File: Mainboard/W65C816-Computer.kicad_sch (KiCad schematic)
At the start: 103 parts, among them J1 ADDR_DATA_DBG, J2 CTRL_BANK_DBG, J3 CPU_MISC_DBG, J4 PJ-102A, J5 DAUGHTER_PWR_AUX, J6 ISA16_DAUGHTER_BUS, Q1 P-MOSFET_REV_PROT_TO220, SW1 RESET, SW2 NMI, SW3 MAIN_PWR_SW_EXT, U1 W65C816S6PG-14, U10 SN74HC04N, U11 SN74HC08N, U12 SN74HC139N, U2 SN74HC573N, U20 AS6C1008-55PCN, U21 AS6C1008-55PCN, U22 AS6C1008-55PCN, U23 AS6C1008-55PCN, U24 AS6C4008-55PCN, U25 AS6C4008-55PCN, U26 AS6C4008-55PCN, U27 AS6C4008-55PCN, U3 SN74HC245N, U30 SST39VF040-70-4I-NHE, U4 MCP130-315D, U5 SN74HC14N, U6 SN74HC138N, U7 SN74HC138N, U8 SN74HC138N, U9 SN74HC00N, X1 ECS-P143X-8.000-BN

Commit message: Added 4MiB memory back
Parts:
- U20, U21, U22, U23: value AS6C1008-55PCN -> AS6C4008-55PCN
- U24, U25, U26, U27: footprint (none) -> Package_DIP:DIP-32_W15.24mm_Socket_LongPads

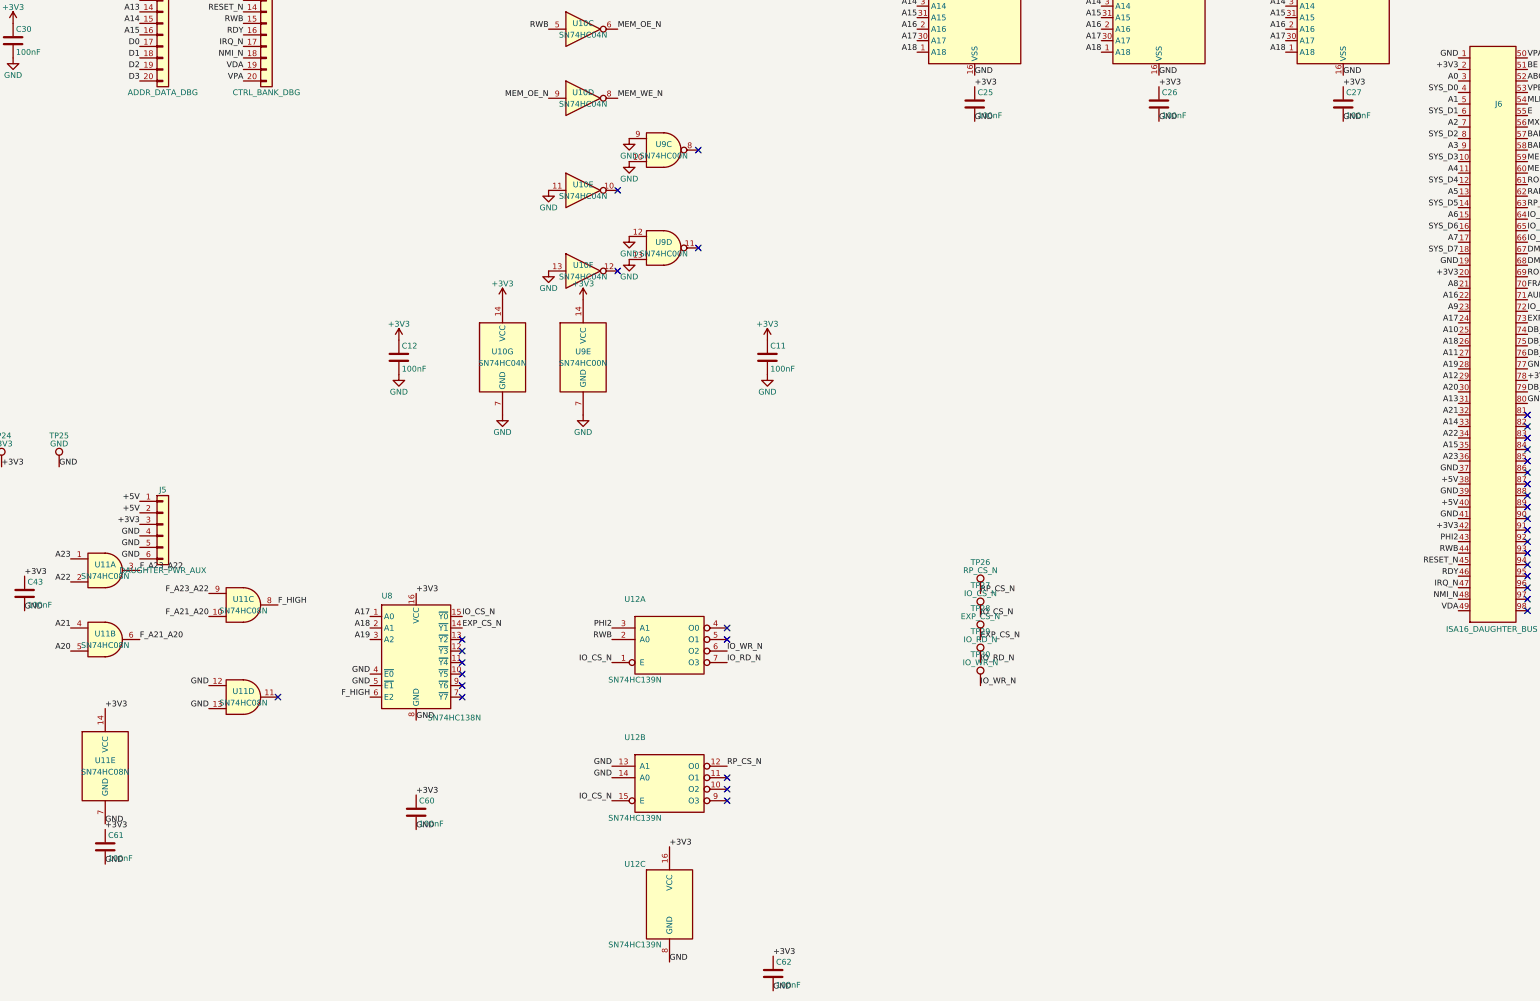
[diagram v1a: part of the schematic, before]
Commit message: Fixed gates
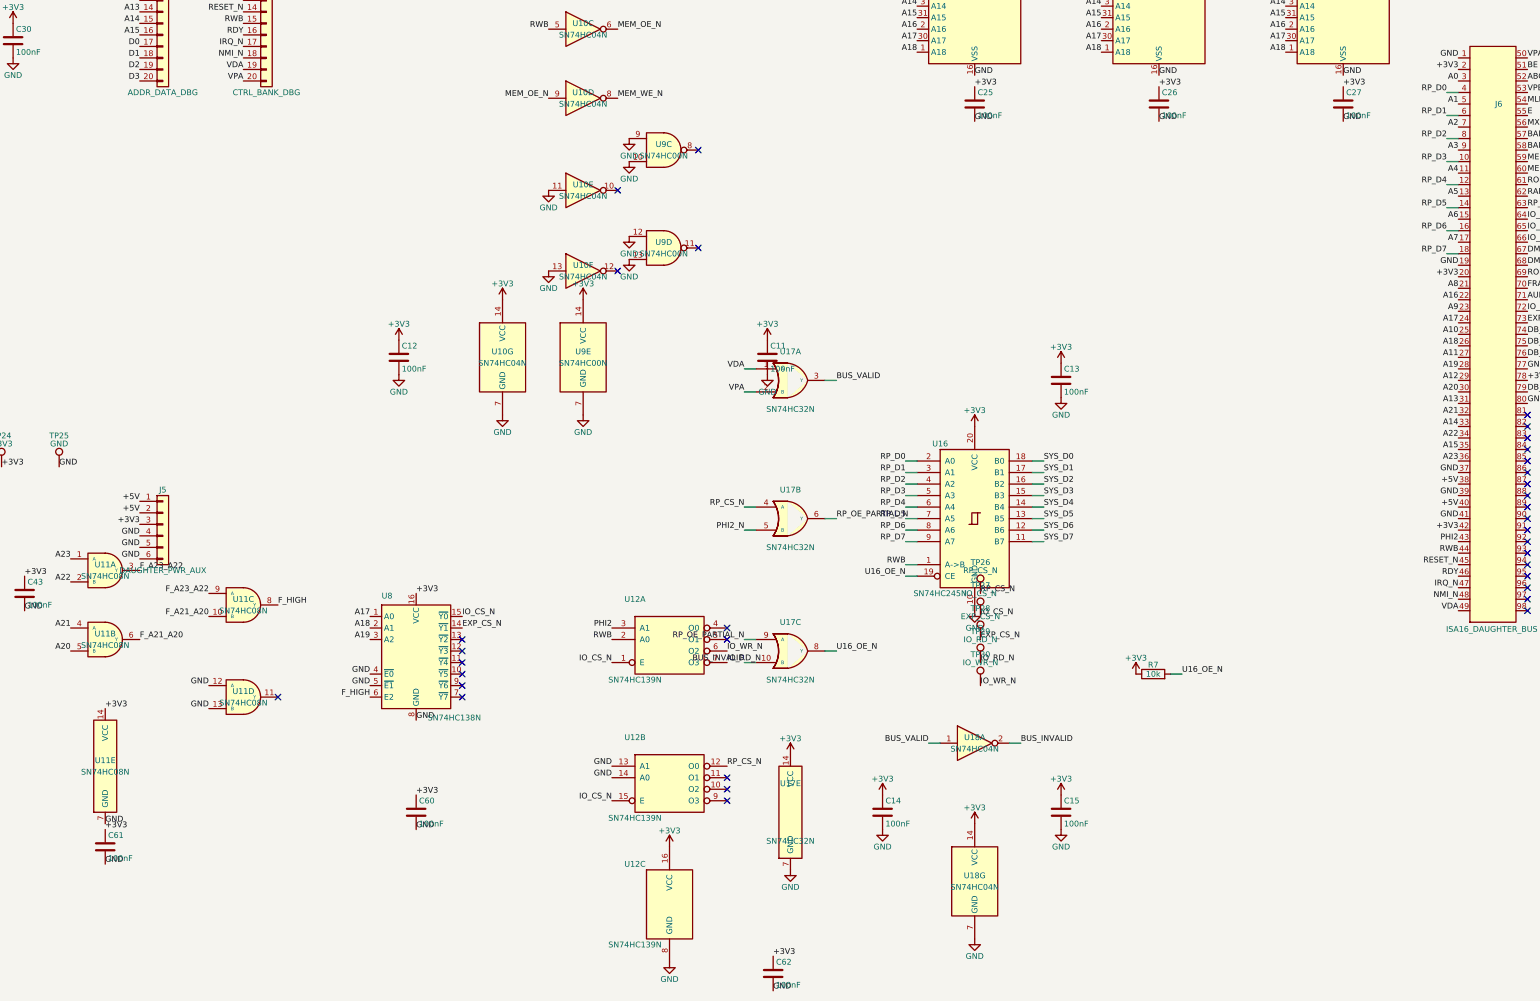
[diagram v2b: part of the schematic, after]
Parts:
- added C13, C14, C15: 100nF, symbol Device:C
- added R7: 10k, symbol Device:R
- added U16: SN74HC245N, symbol 74xx:74HC245
- added U17: SN74HC32N, symbol W65C816-Computer:74HC32
- added U18: SN74HC04N, symbol 74xx:74HC04
- U11: symbol 74xx:74LS08 -> W65C816-Computer:74HC08
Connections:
- net +3V3: now also C13.1, C14.1, C15.1, R7.1, U16.20 (VCC), U17.14 (VCC), U18.14 (VCC)
- net GND: now also C13.2, C14.2, C15.2, U16.10 (GND), U17.7 (GND), U18.7 (GND)
- net PHI2_N: now also U17.5 (B)
- net RP_CS_N: now also U17.4 (A)
- net RWB: now also U16.1 (A->B)
- net SYS_D0: now also U16.18 (B0); no longer J6.4
- net SYS_D1: now also U16.17 (B1); no longer J6.6
- net SYS_D2: now also U16.16 (B2); no longer J6.8
- net SYS_D3: now also U16.15 (B3); no longer J6.10
- net SYS_D4: now also U16.14 (B4); no longer J6.12
- net SYS_D5: now also U16.13 (B5); no longer J6.14
- net SYS_D6: now also U16.12 (B6); no longer J6.16
- net SYS_D7: now also U16.11 (B7); no longer J6.18
- net VDA: now also U17.1 (A)
- net VPA: now also U17.2 (B)
- new net BUS_INVALID: U17.10 (B), U18.2
- new net BUS_VALID: U17.3 (Y), U18.1
- new net RP_D0: J6.4, U16.2 (A0)
- new net RP_D1: J6.6, U16.3 (A1)
- new net RP_D2: J6.8, U16.4 (A2)
- new net RP_D3: J6.10, U16.5 (A3)
- new net RP_D4: J6.12, U16.6 (A4)
- new net RP_D5: J6.14, U16.7 (A5)
- new net RP_D6: J6.16, U16.8 (A6)
- new net RP_D7: J6.18, U16.9 (A7)
- new net RP_OE_PARTIAL_N: U17.6 (Y), U17.9 (A)
- new net U16_OE_N: R7.2, U16.19 (CE), U17.8 (Y)

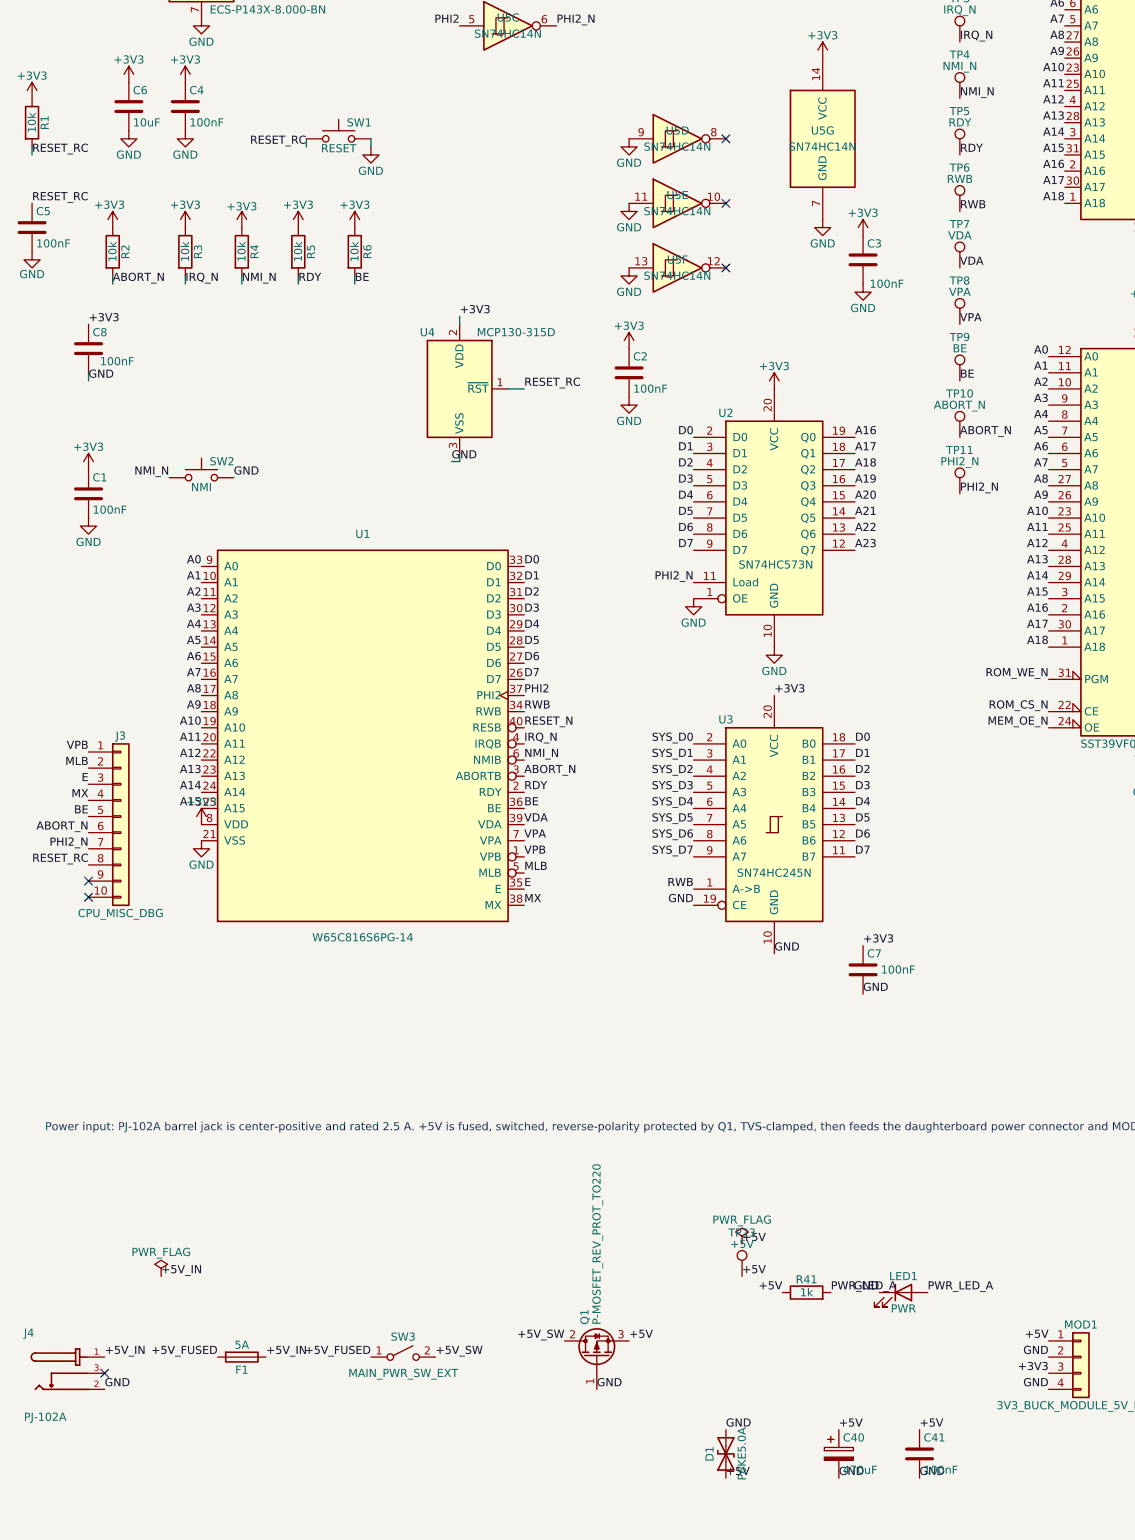
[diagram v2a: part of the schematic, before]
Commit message: replaced switches and plugs with headers
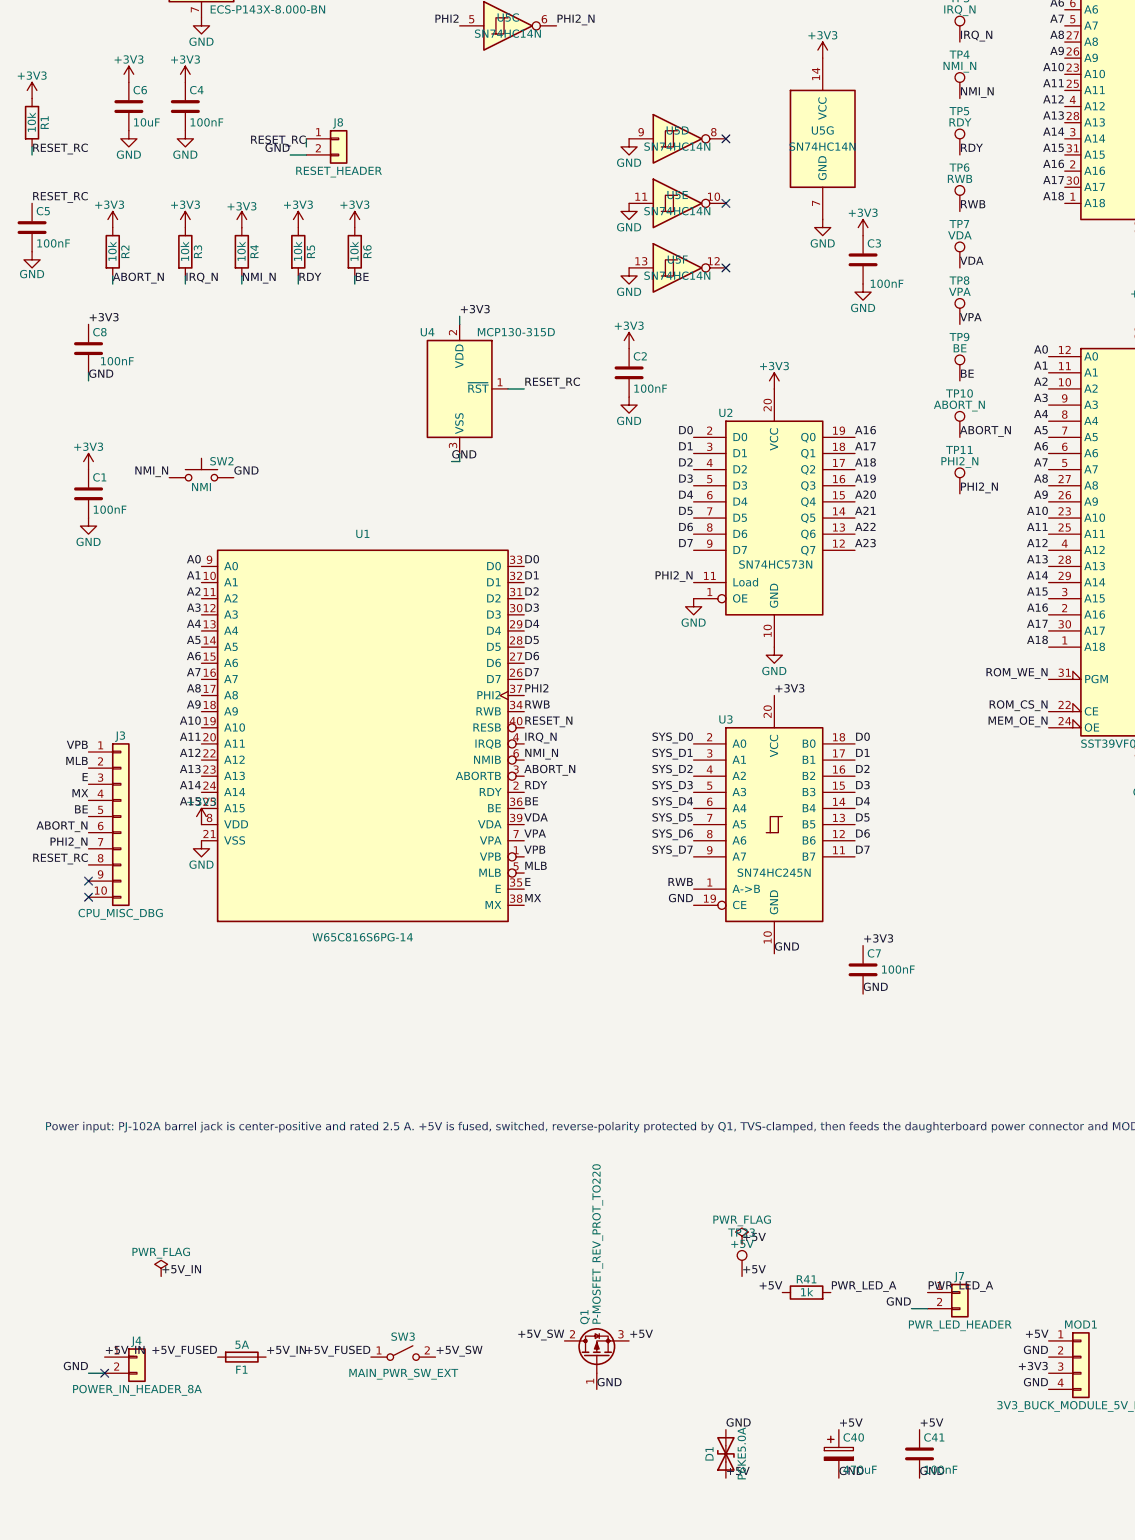
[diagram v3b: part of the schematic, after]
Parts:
- removed J4: PJ-102A, PJ-102A:CUI_PJ-102A, symbol PJ-102A:PJ-102A
- removed LED1: PWR, LED_THT:LED_D5.0mm, symbol Device:LED
- removed SW1: RESET, Button_Switch_THT:SW_PUSH_6mm_H4.3mm, symbol Switch:SW_Push
- added J4: POWER_IN_HEADER_8A, Connector_Phoenix_MC_HighVoltage:PhoenixContact_MCV_1,5_2-GF-5.08_1x02_P5.08mm_Vertical_ThreadedFlange_MountHole, symbol Connector_Generic:Conn_01x02
- added J7: PWR_LED_HEADER, Connector_PinHeader_2.54mm:PinHeader_1x02_P2.54mm_Vertical, symbol Connector_Generic:Conn_01x02
- added J8: RESET_HEADER, Connector_PinHeader_2.54mm:PinHeader_1x02_P2.54mm_Vertical, symbol Connector_Generic:Conn_01x02
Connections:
- net +5V_IN: now also J4.1 (Pin_1)
- net GND: now also J4.2 (Pin_2), J7.2 (Pin_2), J8.2 (Pin_2)
- net PWR_LED_A: now also J7.1 (Pin_1)
- net RESET_RC: now also J8.1 (Pin_1)
